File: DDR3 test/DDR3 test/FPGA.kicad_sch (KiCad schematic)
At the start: 1 part, among them U3 XC7Z010-1CLG225I

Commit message: Resistor Footprints
- Fixed resistor footprints
- Re-added 3D models
- Routed 1.5V reg
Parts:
- U3: footprint Sync_VT extras:225-LFBGA -> Sync_VT extras:BGA225C80P15X15_1300X1300X150N
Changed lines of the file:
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@@
 			)
 		)
-		(property "Footprint" "Sync_VT extras:225-LFBGA"
+		(property "Footprint" "Sync_VT extras:BGA225C80P15X15_1300X1300X150N"
 			(at 60.96 62.23 0)
 			(effects
@@
 			)
 		)
-		(property "Footprint" "Sync_VT extras:225-LFBGA"
+		(property "Footprint" "Sync_VT extras:BGA225C80P15X15_1300X1300X150N"
 			(at 62.23 135.89 0)
 			(effects
@@
 			)
 		)
-		(property "Footprint" "Sync_VT extras:225-LFBGA"
+		(property "Footprint" "Sync_VT extras:BGA225C80P15X15_1300X1300X150N"
 			(at 237.49 77.47 0)
 			(effects

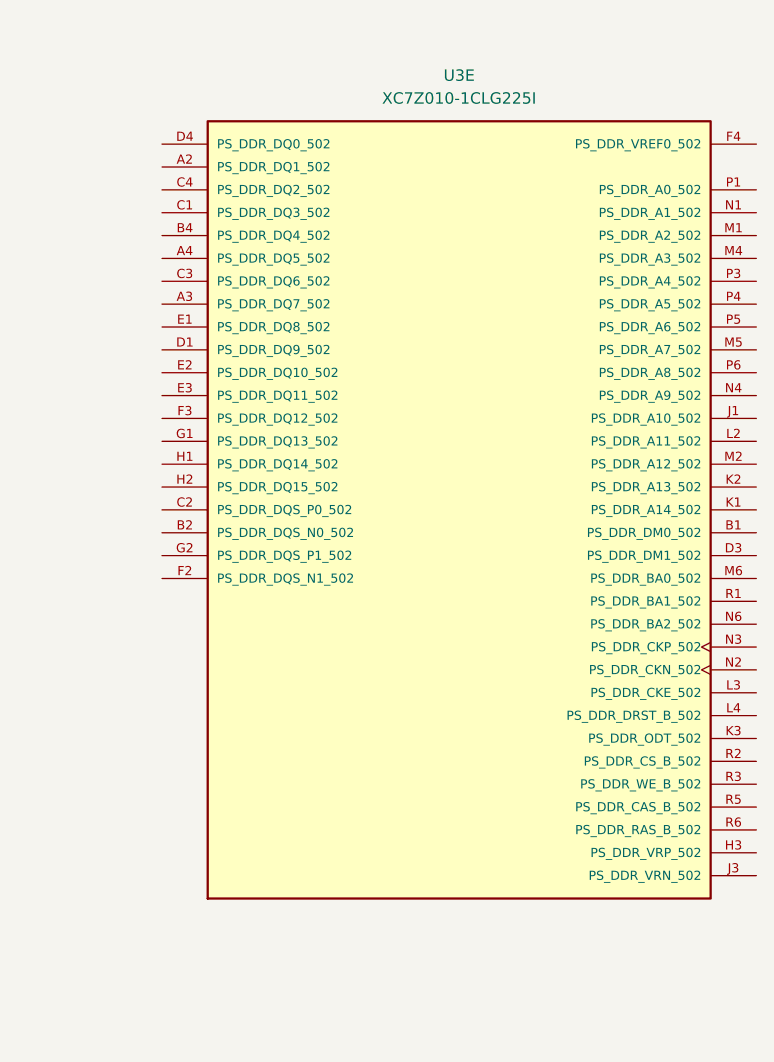
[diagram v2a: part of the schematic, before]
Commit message: pin assignments
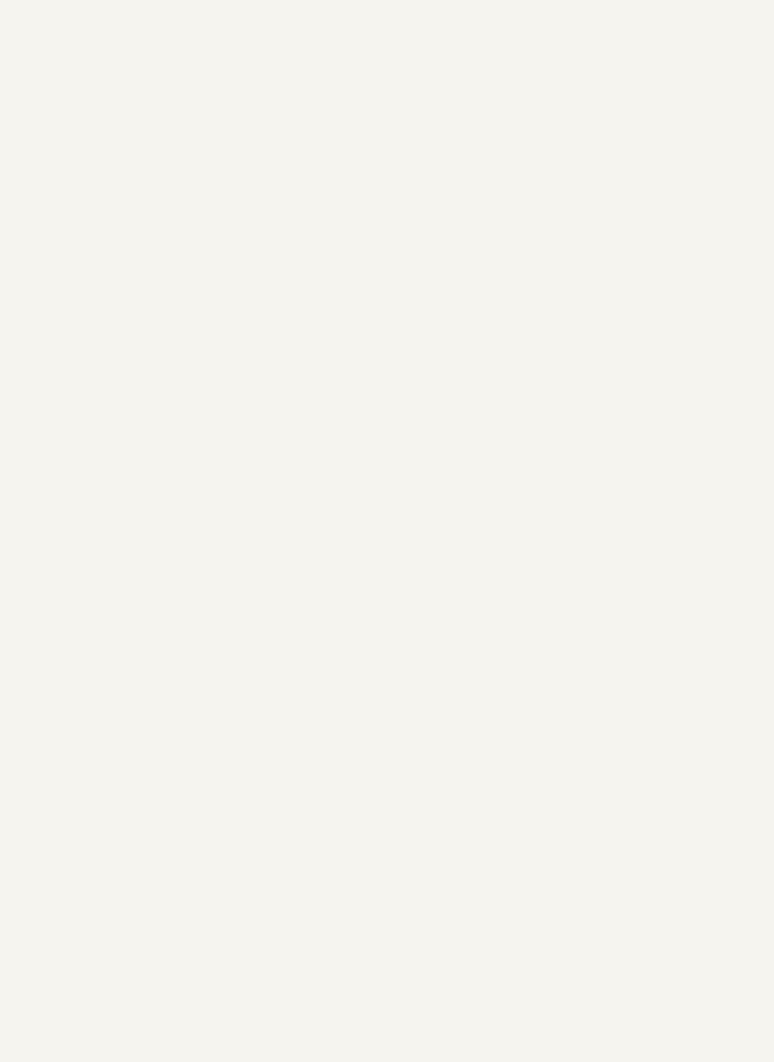
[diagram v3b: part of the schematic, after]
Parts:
- removed unit 5 of U3
